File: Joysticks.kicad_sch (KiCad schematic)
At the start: 0 parts

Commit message: added joystick inputs
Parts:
- added C23, C24, C25, C26: 100nF, 0_capacitors:C_0402_1005Metric, symbol 0_capacitors:CL05B104KO5NNNC
- added R16, R17, R18, R19: 0Ω, 0_resistors:R_0402_1005Metric, symbol 0_resistors:0402WGF0000TCE
- added RV1: LeftX, 0_connectors:JST_PH_B3B-PH-K_1x03_P2.00mm_Vertical, symbol 0_modules:R_Potentiometer
- added RV2: LeftY, 0_connectors:JST_PH_B3B-PH-K_1x03_P2.00mm_Vertical, symbol 0_modules:R_Potentiometer
- added RV3: RightX, 0_connectors:JST_PH_B3B-PH-K_1x03_P2.00mm_Vertical, symbol 0_modules:R_Potentiometer
- added RV4: RightY, 0_connectors:JST_PH_B3B-PH-K_1x03_P2.00mm_Vertical, symbol 0_modules:R_Potentiometer
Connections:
- new net +3.3V: RV1.1, RV2.1, RV3.1, RV4.1
- new net ADC1_INP16: C26.1, R19.1
- new net ADC1_INP4: C23.1, R16.1
- new net ADC1_INP7: C24.1, R17.1
- new net ADC1_INP8: C25.1, R18.1
- new net GND: C23.2, C24.2, C25.2, C26.2, RV1.3, RV2.3, RV3.3, RV4.3
- new net LX: R16.2, RV1.2
- new net LY: R17.2, RV2.2
- new net RX: R18.2, RV3.2
- new net RY: R19.2, RV4.2
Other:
- title: (none) -> UI - Joysticks

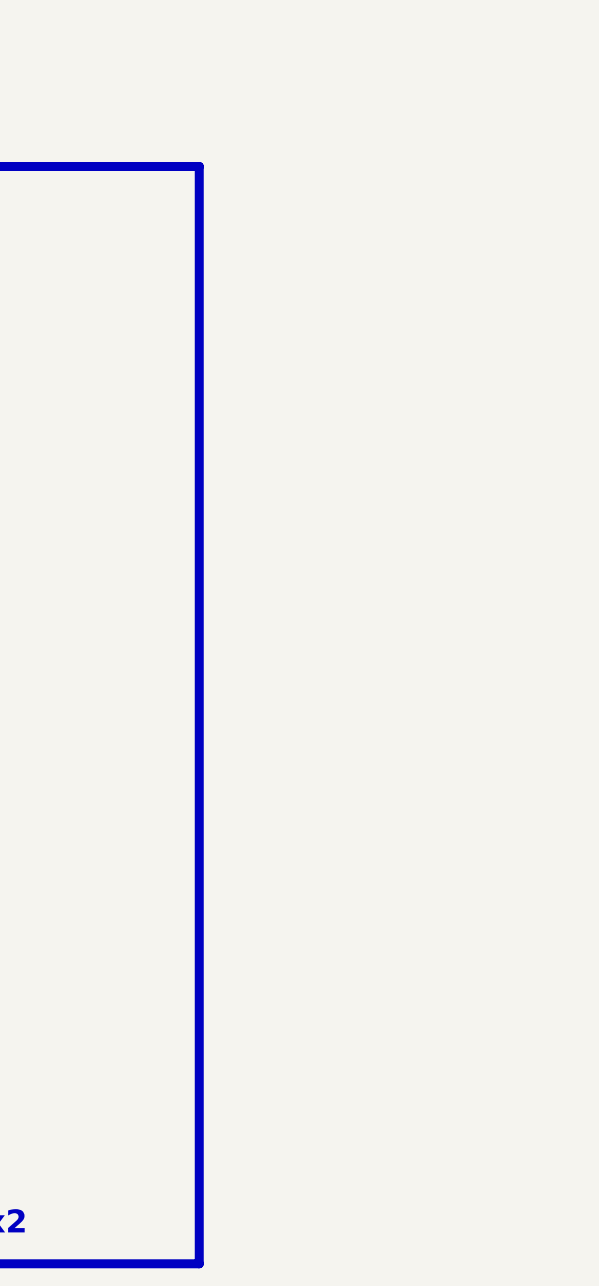
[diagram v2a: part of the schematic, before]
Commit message: added fiducal markers, mounting holes, testpoints
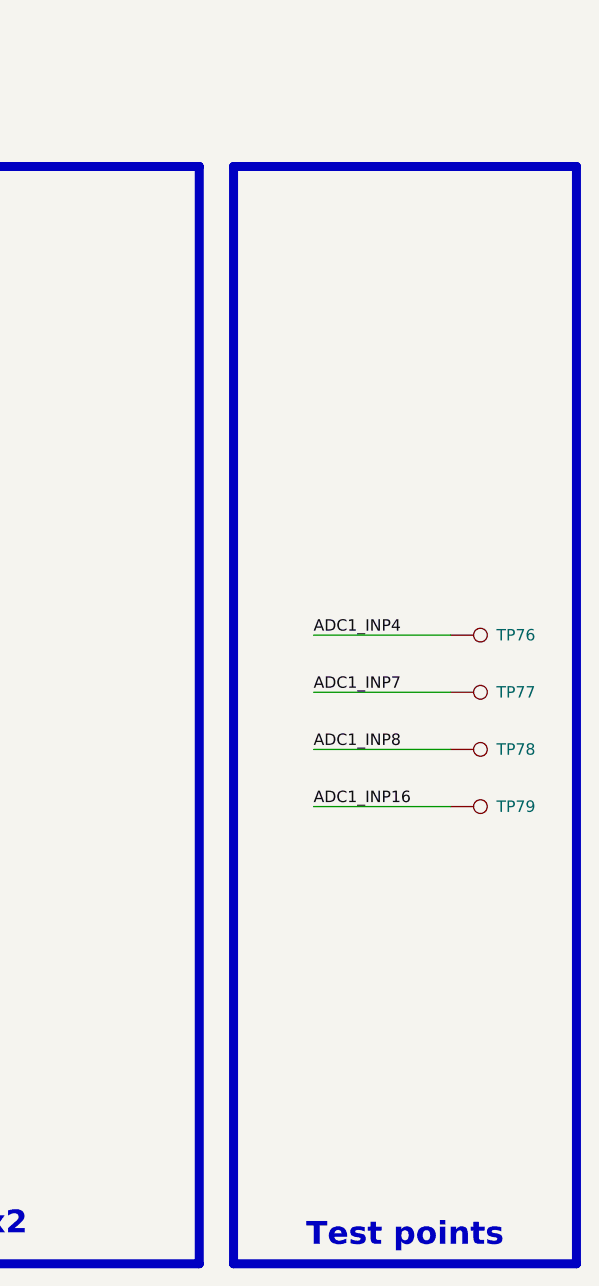
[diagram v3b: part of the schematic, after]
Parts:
- added TP76, TP77, TP78, TP79: TestPoint, 0_pads:TestPoint_Pad_D0.4mm_Back, symbol Connector:TestPoint
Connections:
- net ADC1_INP16: now also TP79.1
- net ADC1_INP4: now also TP76.1
- net ADC1_INP7: now also TP77.1
- net ADC1_INP8: now also TP78.1

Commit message: test points, colors, drc
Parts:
- TP76, TP77, TP78, TP79: footprint 0_pads:TestPoint_Pad_D0.4mm_Back -> 0_pads:TestPoint_Pad_D0.5mm_Back
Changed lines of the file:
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@@
 			)
 		)
-		(property "Footprint" "0_pads:TestPoint_Pad_D0.4mm_Back"
+		(property "Footprint" "0_pads:TestPoint_Pad_D0.5mm_Back"
 			(at 356.87 130.81 0)
 			(effects
@@
 			)
 		)
-		(property "Footprint" "0_pads:TestPoint_Pad_D0.4mm_Back"
+		(property "Footprint" "0_pads:TestPoint_Pad_D0.5mm_Back"
 			(at 356.87 143.51 0)
 			(effects
@@
 			)
 		)
-		(property "Footprint" "0_pads:TestPoint_Pad_D0.4mm_Back"
+		(property "Footprint" "0_pads:TestPoint_Pad_D0.5mm_Back"
 			(at 356.87 137.16 0)
 			(effects
@@
 			)
 		)
-		(property "Footprint" "0_pads:TestPoint_Pad_D0.4mm_Back"
+		(property "Footprint" "0_pads:TestPoint_Pad_D0.5mm_Back"
 			(at 356.87 124.46 0)
 			(effects

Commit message: designator chagnes and cleanup silkscreen
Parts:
- C23, C24, C25, C26: LCSC PN (none) -> C1525
- R16, R17, R18, R19: LCSC PN (none) -> C17168
- RV1, RV2, RV3, RV4: LCSC PN (none) -> C131339
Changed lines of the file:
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@@
+			)
+		)
+		(property "LCSC PN" "C1525"
+			(at 257.81 144.78 0)
+			(effects
+				(font
+					(size 1.27 1.27)
+				)
+				(hide yes)
 			)
 		)
@@
 			)
 		)
+		(property "LCSC PN" "C131339"
+			(at 154.94 140.97 0)
+			(effects
+				(font
+					(size 1.27 1.27)
+				)
+				(hide yes)
+			)
+		)
 		(pin "3"
 		)
@@
 			)
 		)
+		(property "LCSC PN" "C17168"
+			(at 266.7 109.22 0)
+			(effects
+				(font
+					(size 1.27 1.27)
+				)
+				(hide yes)
+			)
+		)
 		(pin "2"
 		)
@@
 			)
 		)
+		(property "LCSC PN" "C131339"
+			(at 279.4 142.24 0)
+			(effects
+				(font
+					(size 1.27 1.27)
+				)
+				(hide yes)
+			)
+		)
 		(pin "3"
 		)
@@
 			)
 		)
+		(property "LCSC PN" "C131339"
+			(at 154.94 107.95 0)
+			(effects
+				(font
+					(size 1.27 1.27)
+				)
+				(hide yes)
+			)
+		)
 		(pin "3"
 		)
@@
 			)
 		)
+		(property "LCSC PN" "C131339"
+			(at 279.4 109.22 0)
+			(effects
+				(font
+					(size 1.27 1.27)
+				)
+				(hide yes)
+			)
+		)
 		(pin "3"
 		)
@@
 			)
 		)
+		(property "LCSC PN" "C17168"
+			(at 266.7 142.24 0)
+			(effects
+				(font
+					(size 1.27 1.27)
+				)
+				(hide yes)
+			)
+		)
 		(pin "2"
 		)
@@
 			)
 		)
+		(property "LCSC PN" "C1525"
+			(at 257.81 111.76 0)
+			(effects
+				(font
+					(size 1.27 1.27)
+				)
+				(hide yes)
+			)
+		)
 		(pin "1"
 		)
@@
 			)
 		)
+		(property "LCSC PN" "C1525"
+			(at 133.35 143.51 0)
+			(effects
+				(font
+					(size 1.27 1.27)
+				)
+				(hide yes)
+			)
+		)
 		(pin "1"
 		)
@@
 			)
 		)
+		(property "LCSC PN" "C17168"
+			(at 142.24 140.97 0)
+			(effects
+				(font
+					(size 1.27 1.27)
+				)
+				(hide yes)
+			)
+		)
 		(pin "2"
 		)
@@
 			)
 		)
+		(property "LCSC PN" "C17168"
+			(at 142.24 107.95 0)
+			(effects
+				(font
+					(size 1.27 1.27)
+				)
+				(hide yes)
+			)
+		)
 		(pin "2"
 		)
@@
 			(at 133.35 110.49 0)
 			(effects
+				(font
+					(size 1.27 1.27)
+				)
+				(hide yes)
+			)
+		)
+		(property "LCSC PN" "C1525"
+			(at 133.35 110.49 0)
+			(effects
